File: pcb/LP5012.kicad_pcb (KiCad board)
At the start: 2 copper layers, 16.2 x 24.5 mm, 16 parts, among them J1 Main Connector, U1 LP5012

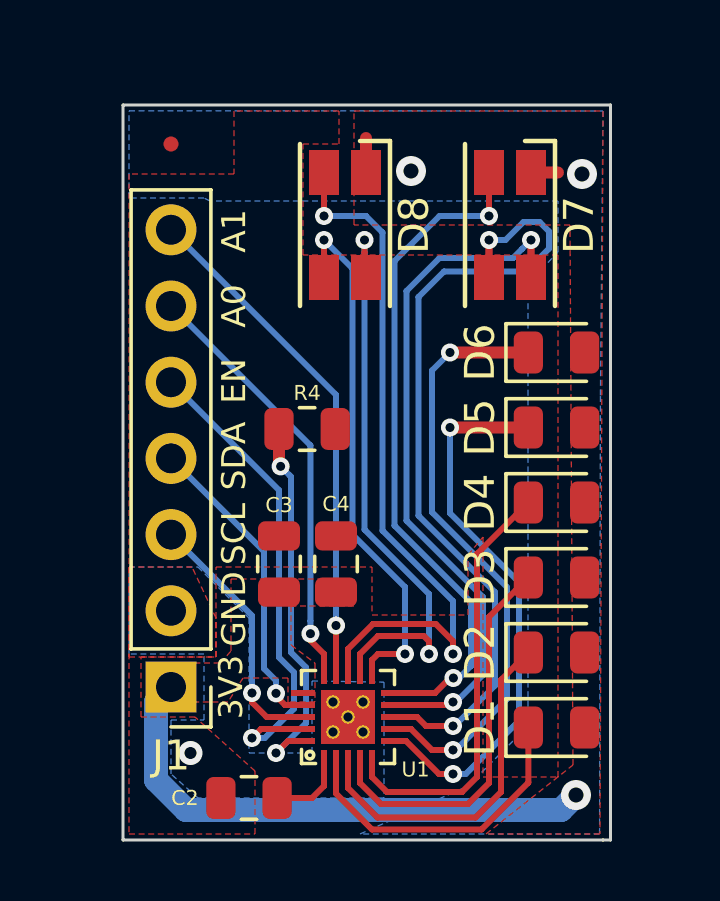
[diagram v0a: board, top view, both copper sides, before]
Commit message: Inclusión de cambios de revisión 2
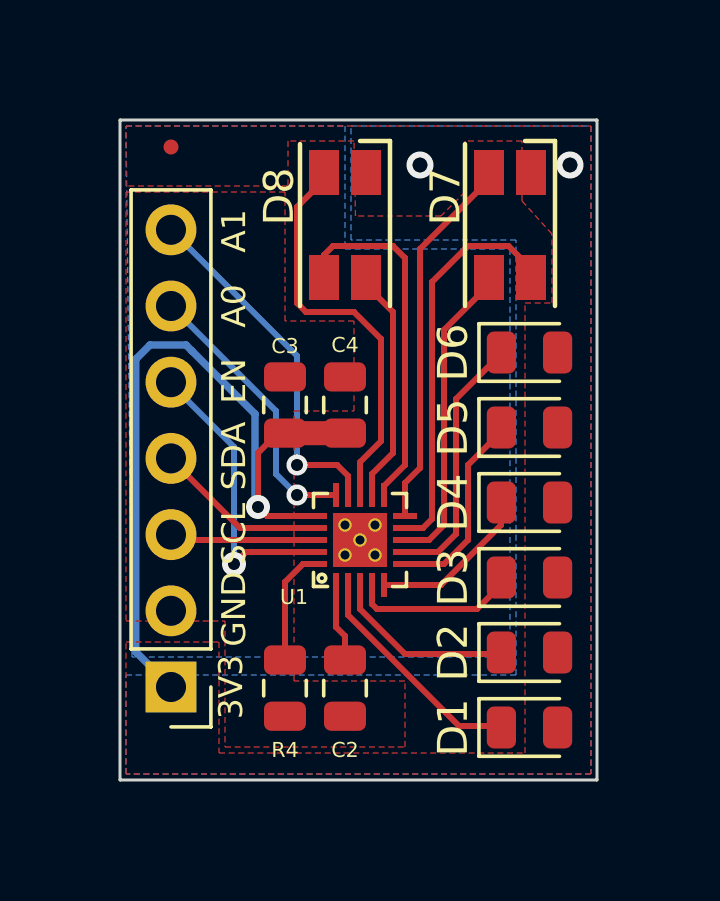
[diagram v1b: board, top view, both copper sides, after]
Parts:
- moved R4 8.67 mm to (145.5, 94.9), turned to 270 degrees
- moved U1 5.91 mm to (148.0, 90.0)
- moved C4 5.31 mm to (147.5, 85.5)
- moved C3 5.30 mm to (145.5, 85.5)
- moved C2 4.86 mm to (147.5, 94.9), turned to 270 degrees
- moved G*** 1.39 mm to (152.3, 89.5)
- moved D1 0.90 mm to (153.7, 96.2)
- moved D2 0.90 mm to (153.7, 93.8)
- moved D3 0.90 mm to (153.7, 91.2)
- moved D4 0.90 mm to (153.7, 88.8)
- moved D5 0.90 mm to (153.7, 86.2)
- moved D6 0.90 mm to (153.7, 83.8)
- moved FD1 0.10 mm to (141.7, 76.9)
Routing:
- net /LB6: track 27.3 -> 10.7 mm, vias 2 -> 0
- net /LB4: track 18.7 -> 6.63 mm, vias 2 -> 0
- net /LB10: track 19.7 -> 7.82 mm, vias 2 -> 0
- net /LB5: track 20.2 -> 8.57 mm, vias 2 -> 0
- net /LB11: track 23.8 -> 13.4 mm, vias 2 -> 0
- net /LB7: track 23.4 -> 13.0 mm, vias 2 -> 0
- net /LB8: track 22.8 -> 12.6 mm, vias 2 -> 0
- net /LB3: track 14.3 -> 5.43 mm
- net Net-(R4-Pad1): track 12.7 -> 3.95 mm, vias 2 -> 0
- net /LB2: track 13.0 -> 5.53 mm
- net VCC: track 20.0 -> 26.7 mm
- net /IN_EN: track 16.2 -> 9.74 mm
- net /LB9: track 17.9 -> 11.5 mm, vias 2 -> 0
- net /LB1: track 11.8 -> 6.12 mm
- net /ADDR0: track 17.1 -> 12.1 mm
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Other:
- board size 16.2 x 24.5 mm -> 15.9 x 22 mm
- board text added: "Fabricante elegido: PCBWay Origen: China Configuraciones sin costo adicional: Mínimo ancho de pista: 6mil (0.153mm) Mínima distacia entre pista: 6mil (0.153) Mínimo diámetro de perforacion: 0.3mm Terminación: HASL con plmo"
- board text added: "Terminación superficial: HASL con plomo Grosor: 1.6mm Materíal: FR4 TG130-140 Color de Máscara de soldadura: Verde Color de Serigrafía: Blanco Mínimo ancho de pista: 0.2mm Mínimo diámetro de perforación: 0.4mm Conector con PTH Margen de zonas de cobre: 0.1mm Grilla utilizada: 0.1mm"
- board text removed: "Terminación superficial: HASL con plomo Grosor: 1.6mm Materíal: FR4 TG130-140 Color de Máscara de soldadura: Verde Color de Serigrafía: Blanco Mínimo ancho de pista: 0.2mm Mínimo diámetro de perforación: 0.3mm Grilla utilizada: 0.1mm"

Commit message: Ultimas modificaciones
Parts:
- moved G*** 1.15 mm to (152.4, 88.3)
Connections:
- net /LB0 renamed /LED0
- net /LB1 renamed /LED1
- net /LB10 renamed /LED10
- net /LB11 renamed /LED11
- net /LB2 renamed /LED2
- net /LB3 renamed /LED3
- net /LB4 renamed /LED4
- net /LB5 renamed /LED5
- net /LB6 renamed /LED6
- net /LB7 renamed /LED7
- net /LB8 renamed /LED8
- net /LB9 renamed /LED9
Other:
- board size 15.9 x 22 mm -> 16 x 22 mm

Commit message: Inclusión del agujero requerido
Inclusión de agujero para sujeción M2
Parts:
- moved FD1 3.10 mm to (144.8, 77.0)
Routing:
- net (no net): vias 0 -> 1
